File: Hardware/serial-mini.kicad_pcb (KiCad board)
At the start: 4 copper layers, 97 x 42 mm, 82 parts, among them J1 PICKIT V3 Header, J2 10103593-0001LF, J3 Serial Port, Q1 IRLML2060, Q2 IRLML2060, Q3 IRLML2060, U1 MAX232, U2 SN74AHC14RGYR, U3 DSPIC33CK64MP102, U4 MIC5504-3.3YM5-TR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

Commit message: Add BOM
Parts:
- D1, D2, D3: value LED -> CLVBA-FKA
- FB1: value Ferrite_Bead_Small -> MI0805K601R
- J1: value PICKIT V3 Header -> 801-47-006-10-012000
- J3: value Serial Port -> 3-106505-2
- U1: value MAX232 -> MAX232ECPWR

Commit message: Fix PRTR5V0U2F footprint
Footprint was flipped wrong way on PCB, also removed BOM folder since it messed up Linguist
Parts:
- R12, R14, R16: value 155 -> 150
- moved C12 1.91 mm to (161.3, 84.6), turned to 0 degrees
- moved R21 0.63 mm to (157.5, 84.7), turned to 270 degrees
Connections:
- D6 pad 1: /USB to UART/D+ -> /USB to UART/D-
- D6 pad 3: /USB to UART/D- -> /USB to UART/D+
- R21 pad 2: Net-(C12-Pad2) -> Net-(C13-Pad1)
- R22 pad 2: Net-(C13-Pad1) -> Net-(C12-Pad2)
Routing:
- net Net-(C12-Pad2): track 10.1 -> 12.3 mm, vias 2 -> 0
- net GND: track 86.0 -> 87.1 mm, vias 33 -> 32
- net /USB to UART/3V@20mA: track 29.2 -> 29.9 mm
- net Net-(C13-Pad1): track 12.5 -> 13.0 mm

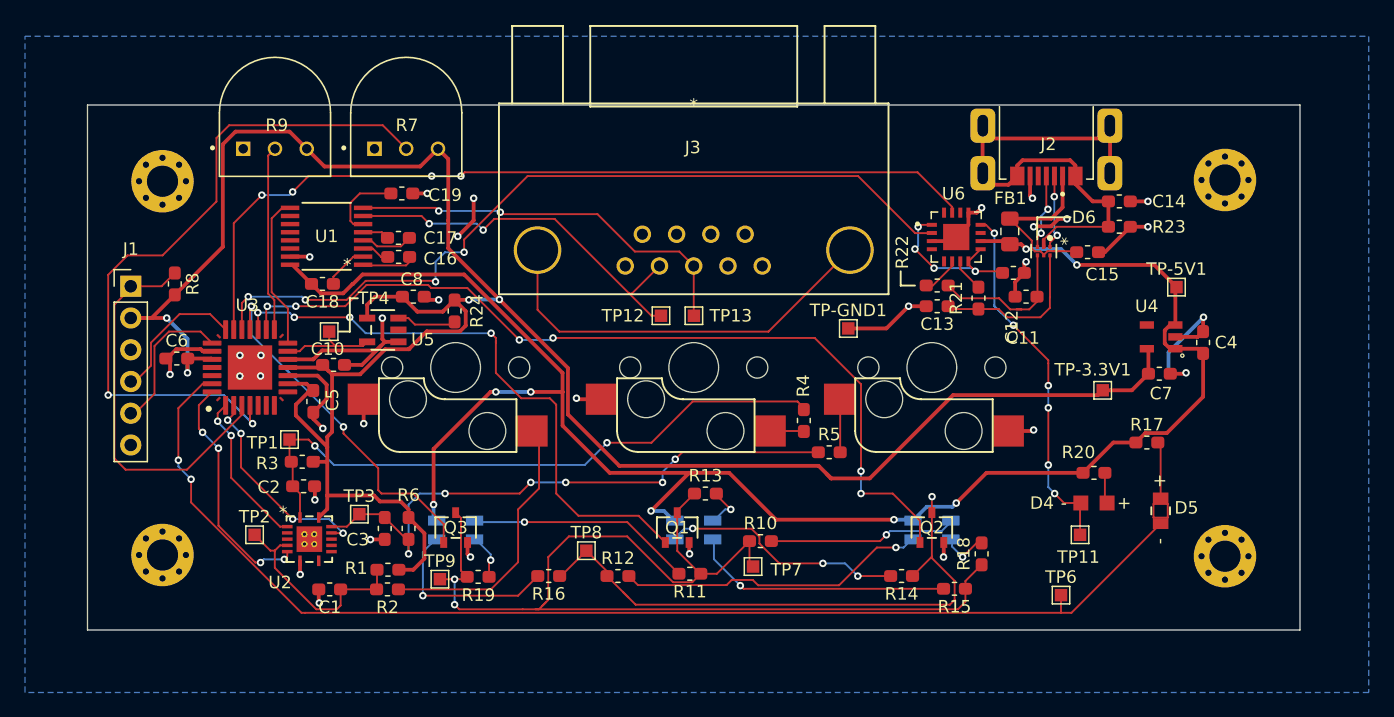
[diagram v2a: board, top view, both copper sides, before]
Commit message: Make leadless package pads longer, add vias
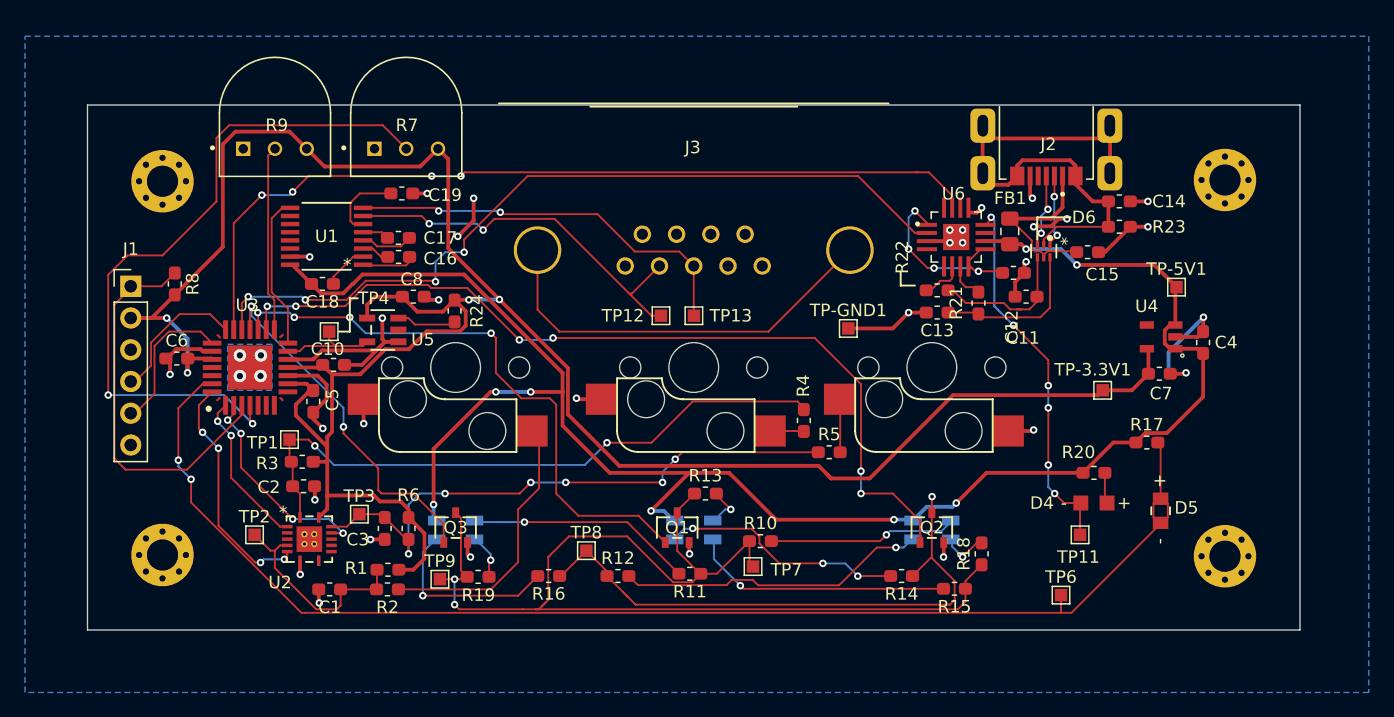
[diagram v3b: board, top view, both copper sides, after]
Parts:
- D5: value VAOL-S8WR4 -> LED_VCCLITE_0805_VCC
- J3: value 3-106505-2 -> CONN_3-106505-2_TYCO
- U1: value MAX232ECPWR -> PW16_TEX
- U2: value SN74AHC14RGYR -> RGY14_2P05X2P05
- U5: value SIT2001BI-S2-33S-100.000000D -> SOT_SiT1630-S
- moved C13 0.51 mm to (154.2, 85.9)
- moved R21 0.40 mm to (157.5, 85.1)
- moved R22 0.39 mm to (154.2, 84.1)
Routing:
- net Net-(C11-Pad1): track 13.2 -> 16.6 mm
- net GND: track 87.1 -> 84.5 mm, vias 32 -> 36
- net Net-(R21-Pad1): track 2.66 -> 3.46 mm
- net /USB to UART/3V@20mA: track 29.9 -> 30.7 mm
- net /UART-TX: track 69.3 -> 70.0 mm
- net /Blue: track 29.4 -> 28.7 mm
- net Net-(R22-Pad1): track 3.09 -> 3.81 mm
